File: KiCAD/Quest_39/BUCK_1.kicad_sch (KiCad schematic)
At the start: 32 parts, among them U10 LTM4611EV-PBF, U11 MCP4151-502E/SN, U8 AD626ANZ, U9 INA226

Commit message: Fixed INA226 schem. mistake and further layout work
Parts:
- added C33: 100nF, Capacitor_SMD:C_0603_1608Metric, symbol Device:C
- renumbered C28 to C29, C29 to C30, C30 to C31, C31 to C32, C32 to C34, C33 to C35, C34 to C36, C35 to C37, C36 to C38, C37 to C39, C38 to C40, C39 to C41, C40 to C42, C41 to C43
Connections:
- net +5V: now also C33.1
- net GND: now also C33.2
- net PV_POS: no longer C29.1, C30.1, C31.1, C32.1, R24.2, R26.1, R29.1, U10.A1 (VIN), U10.A2 (VIN), U10.A3 (VIN), U10.A4 (VIN), U10.A5 (VIN), U10.A6 (VIN), U10.B1 (VIN), U10.B2 (VIN), U10.B3 (VIN), U10.B4 (VIN), U10.B5 (VIN), U10.B6 (VIN), U10.C1 (VIN), U10.C2 (VIN), U10.C3 (VIN), U10.C4 (VIN), U10.C5 (VIN), U10.C6 (VIN)
- net Vin-: no longer TP14.1, U8.5 (OUT), U9.8 (Vbus)
- new net: TP14.1, U8.5 (OUT), U9.8 (Vbus)
- new net BUCK_VIN: C29.1, C30.1, C31.1, C32.1, R24.2, R26.1, R29.1, U10.A1 (VIN), U10.A2 (VIN), U10.A3 (VIN), U10.A4 (VIN), U10.A5 (VIN), U10.A6 (VIN), U10.B1 (VIN), U10.B2 (VIN), U10.B3 (VIN), U10.B4 (VIN), U10.B5 (VIN), U10.B6 (VIN), U10.C1 (VIN), U10.C2 (VIN), U10.C3 (VIN), U10.C4 (VIN), U10.C5 (VIN), U10.C6 (VIN)

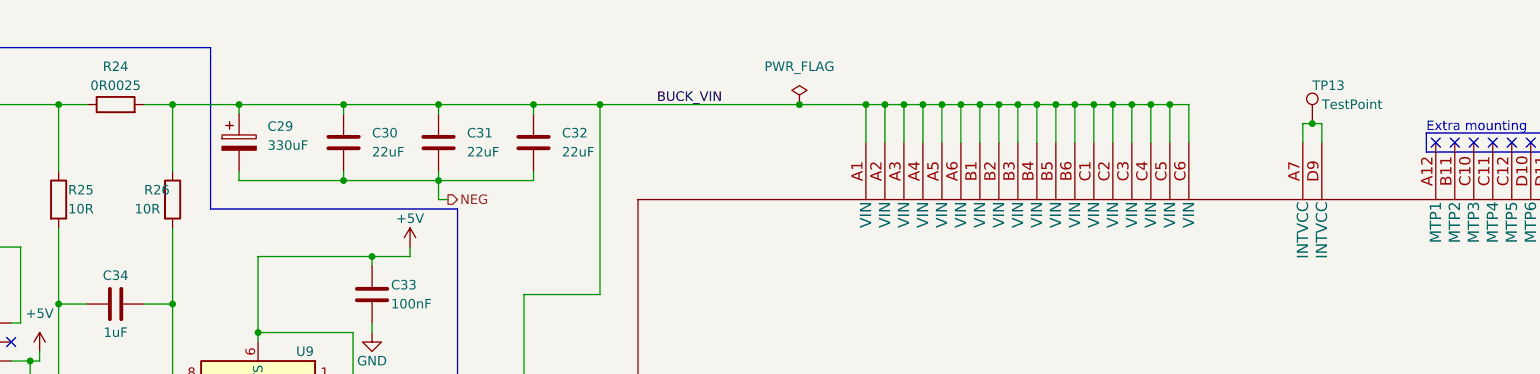
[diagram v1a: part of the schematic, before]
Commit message: Partial wiring of first buck converter section PCB layout
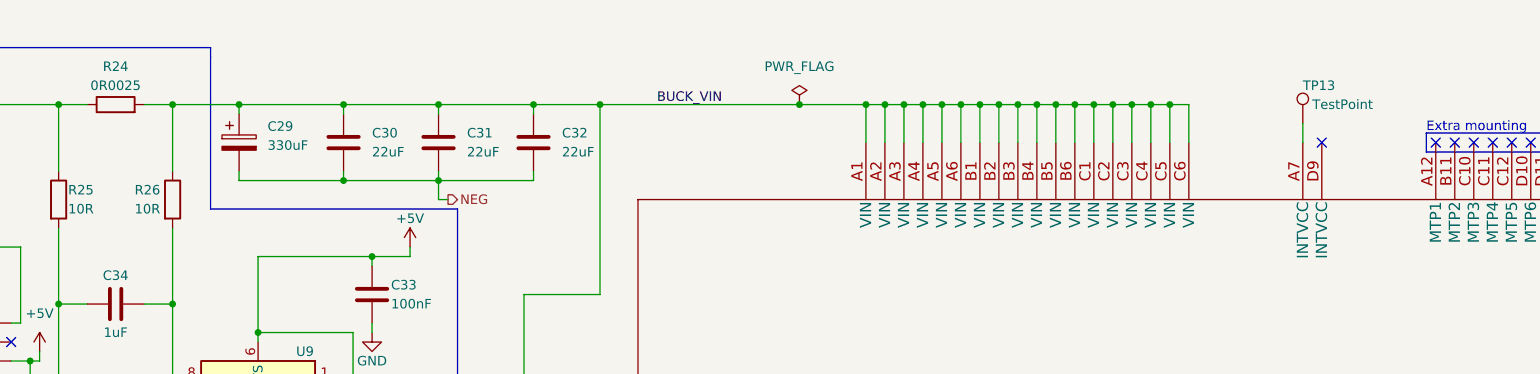
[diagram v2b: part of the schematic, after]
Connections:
- net at TP13.1, U10.A7 (INTVCC): no longer U10.D9 (INTVCC)
- no-connect marks 12 -> 13

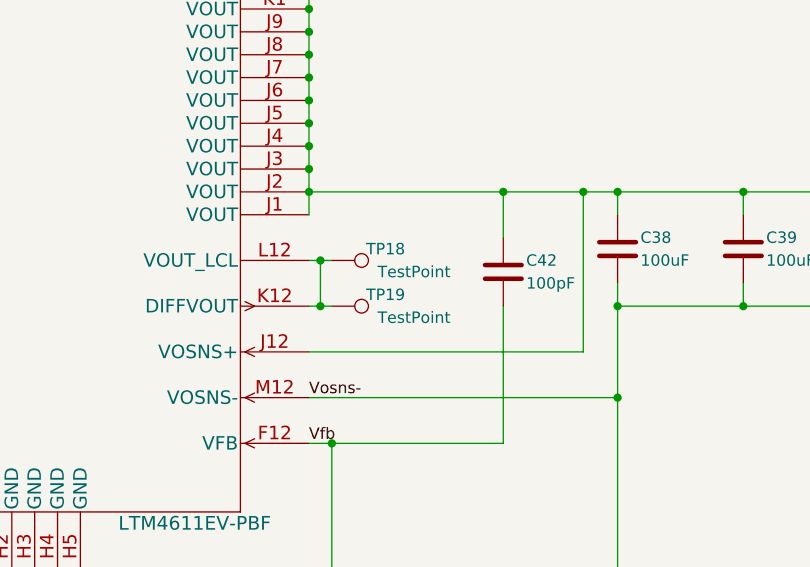
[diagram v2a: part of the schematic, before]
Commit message: Added 3rd buck converter section
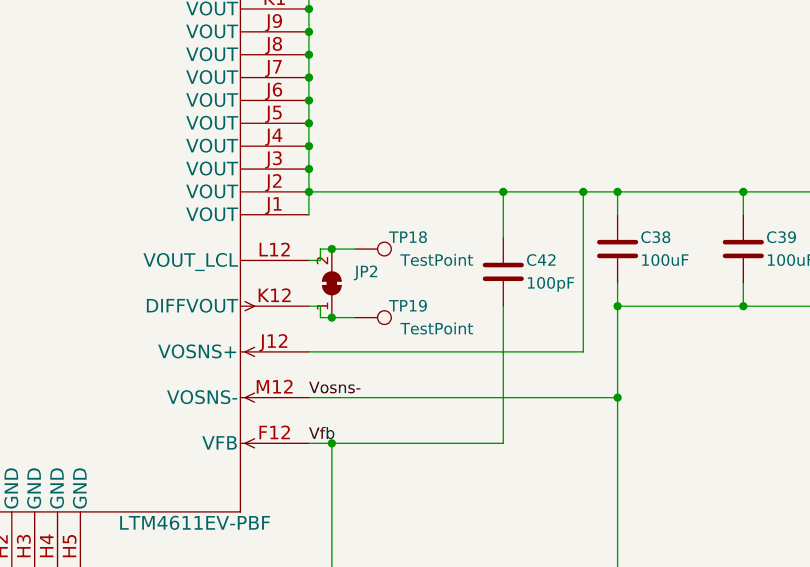
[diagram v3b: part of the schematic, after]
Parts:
- added JP2: SolderJumper_2_Bridged, Jumper:SolderJumper-2_P1.3mm_Bridged_RoundedPad1.0x1.5mm, symbol Jumper:SolderJumper_2_Bridged
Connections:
- net at TP19.1, U10.K12 (DIFFVOUT): now also JP2.1 (A); no longer TP18.1, U10.L12 (VOUT_LCL)
- new net: JP2.2 (B), TP18.1, U10.L12 (VOUT_LCL)
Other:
- moved on the sheet: TP18, TP19
